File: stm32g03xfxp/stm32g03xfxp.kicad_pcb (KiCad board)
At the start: 2 copper layers, 17.8 x 33 mm, 17 parts, among them J1 USB2.0_C_v3, J3 ProMicro-RightPin, SW1 SW_Push, U1 AMS1117-3.3, U2 STM32G030F6P6

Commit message: up
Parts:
- added G***: LOGO, $74th:74th-5mm, B.Cu at (73.7, 49.0)
- added REF**: twitter, $74th:twitter, B.Cu at (73.9, 52.1)
- moved JP1 0.37 mm to (70.9, 48.3)
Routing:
- net RST: track 0.00 -> 49.8 mm, vias 0 -> 1
- net GND: track 0.00 -> 37.6 mm, vias 0 -> 28
- net 10/A10: track 0.00 -> 36.3 mm, vias 0 -> 2
- net 1/UART_TX: track 0.00 -> 24.4 mm, vias 0 -> 2
- net 0/UART_RX: track 0.00 -> 23.2 mm, vias 0 -> 2
- net 15/SPI_SCK: track 0.00 -> 21.2 mm
- net SWD_CLK: track 0.00 -> 19.2 mm, vias 0 -> 1
- net SWD_DIO: track 0.00 -> 18.5 mm, vias 0 -> 2
- net VCC: track 30.6 -> 48.3 mm
- net 18/A0: track 0.00 -> 15.7 mm, vias 0 -> 1
- net 2/I2C_SDA: track 0.00 -> 14.2 mm, vias 0 -> 1
- net 4/A6: track 0.00 -> 13.9 mm, vias 0 -> 1
- net 3/I2C_SCL: track 0.00 -> 13.5 mm, vias 0 -> 1
- net 6/A7: track 0.00 -> 10.7 mm, vias 0 -> 1
- net 19/A1: track 0.00 -> 10.4 mm
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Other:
- board text added: "3V"
- board text added: "5V"
- board text added: "A0"
- board text added: "A1"
- board text added: "A11"
- board text added: "A12"
- board text added: "A2"
- board text added: "A4"
- board text added: "A5"
- board text added: "A6"
- board text added: "A7"
- board text added: "B0"
- board text added: "B14"
- board text added: "B9"
- board text added: "C15"
- board text added: "CL"
- board text added: "DI"
- board text added: "G"
- board text added: "R"
- board text added: "RT"
- board text added: "SCL"
- board text added: "SDA"
- board text added: "STM32G03xFxP"
- board text added: "STM32G03xFxP ProMicro"
- board text added: "T"
- board text added: "v1.0.0"

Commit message: stm32g03xfxp/v1.0.0
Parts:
- added REF**: JLCJLCJLCJLC, $74th:JLCJLCJLCJLC, B.Cu at (65.4, 47.9)

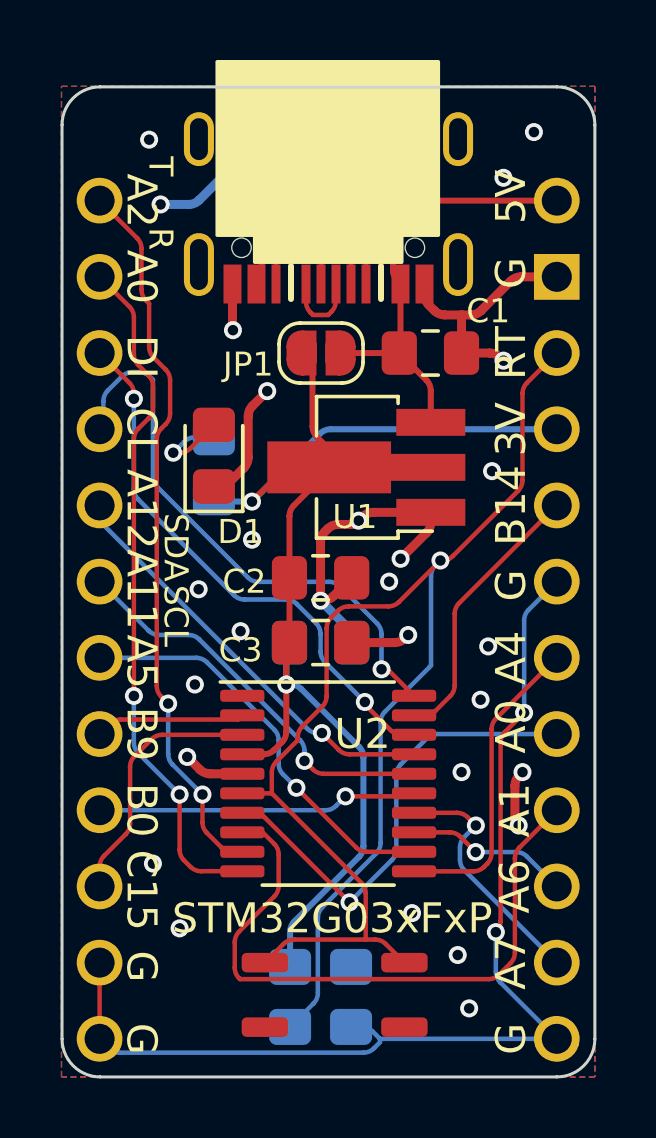
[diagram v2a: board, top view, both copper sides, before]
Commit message: fix dio/clk
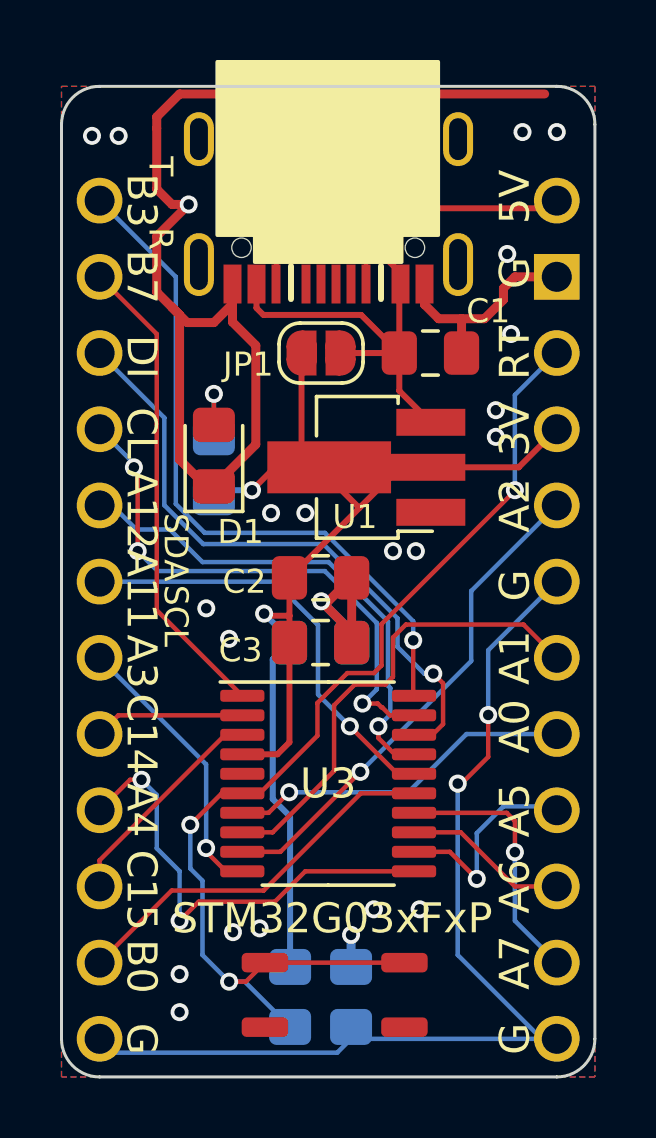
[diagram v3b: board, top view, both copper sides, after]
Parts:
- removed U2: STM32G030F6P6, Package_SO:TSSOP-20_4.4x6.5mm_P0.65mm
- added U3: STM32G030F6Px, Package_SO:TSSOP-20_4.4x6.5mm_P0.65mm, F.Cu at (71.1, 62.6)
- R1: value 200 -> 10k
- renumbered G*** to G1, REF** to T1, REF** to T2
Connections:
- CH1 pad 11: 10/A10 -> 8/A8
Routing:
- net GND: track 37.1 -> 57.6 mm, vias 28 -> 24
- net 15/SPI_SCK: track 21.3 -> 7.08 mm, vias 0 -> 1
- net RST: track 49.4 -> 36.6 mm, vias 1 -> 3
- net 8/A8: track 0.00 -> 12.8 mm
- net 21/A3: track 9.23 -> 16.6 mm, vias 0 -> 1
- net 0/UART_RX: track 23.0 -> 15.9 mm, vias 2 -> 0
- net 19/A1: track 10.3 -> 15.9 mm
- net 6/A7: track 10.7 -> 15.5 mm, vias 1 -> 2
- net 4/A6: track 13.8 -> 9.41 mm
- net 18/A0: track 15.6 -> 11.6 mm
- net VCC: track 48.0 -> 45.2 mm
- net unconnected-(J1-D+-Pad3): track 2.72 -> 0.00 mm
- net unconnected-(J1-D--Pad2): track 2.67 -> 0.00 mm
- net 2/I2C_SDA: track 14.2 -> 16.7 mm
- net SWD_DIO: track 18.3 -> 20.8 mm, vias 2 -> 1
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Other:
- outline, holes or cut-outs redrawn
- board text added: "A3"
- board text added: "B3"
- board text added: "B7"
- board text added: "C14"
- board text added: "v1.1.0"
- board text removed: "B14"
- board text removed: "B9"
- board text removed: "v1.0.0"

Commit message: v1.1.1
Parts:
- removed T1: JLCJLCJLCJLC, $74th:JLCJLCJLCJLC
- removed T2: twitter, $74th:twitter
- C3: moved to B.Cu
- D1: value LED -> Blue
- moved C4 7.71 mm to (73.2, 65.3)
- moved C3 4.89 mm to (73.2, 62.2)
- moved R2 3.56 mm to (72.8, 41.8)
- moved R1 3.56 mm to (69.2, 41.7)
- moved C2 1.66 mm to (72.5, 55.6)
- turned U2 to 180 degrees
- renumbered J3 to J2, R2 to R1, R3 to R2, R1 to R3, R5 to R4, R4 to R5, U3 to U2
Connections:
- U2 pad 5: unconnected-(U3-VSS-Pad5) -> GND
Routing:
- net GND: track 57.6 -> 40.8 mm, vias 24 -> 27
- net 5: track 5.01 -> 20.1 mm, vias 0 -> 1
- net 0/UART_RX: track 15.9 -> 26.5 mm, vias 0 -> 1
- net 15/SPI_SCK: track 7.08 -> 17.5 mm, vias 1 -> 0
- net 14/SPI_MISO: track 5.51 -> 15.6 mm
- net 19/A1: track 15.9 -> 6.05 mm
- net 7: track 7.36 -> 16.1 mm, vias 0 -> 2
- net 21/A3: track 16.6 -> 9.74 mm, vias 1 -> 0
- net 18/A0: track 11.6 -> 5.01 mm, vias 1 -> 0
- net 16/SPI_MOSI: track 8.77 -> 15.3 mm, vias 1 -> 0
- net VCC: track 45.2 -> 51.4 mm, vias 2 -> 6
- net 6/A7: track 15.5 -> 9.74 mm, vias 2 -> 1
- net 2/I2C_SDA: track 16.7 -> 12.9 mm
- net 3/I2C_SCL: track 14.5 -> 11.2 mm
- net 1/UART_TX: track 23.2 -> 26.4 mm, vias 1 -> 2
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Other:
- board text added: "RX"
- board text added: "SCK"
- board text added: "TX"
- board text added: "v1.1.1"
- board text removed: "v1.1.0"

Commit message: v1.2.0
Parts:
- removed JP1: SolderJumper_2_Open, Jumper:SolderJumper-2_P1.3mm_Open_RoundedPad1.0x1.5mm
- added J3: DAPLink-SWD-Recv-6Pin, $74th:BoxPinHeader_2x03_P1.27mm_Vertical, F.Cu at (71.2, 69.3)
- C1, C2, U1: moved to B.Cu
- moved G1 13.8 mm to (66.5, 60.8)
- moved C4 8.77 mm to (73.5, 56.5)
- moved D1 7.39 mm to (74.7, 51.1), turned to 180 degrees
- moved R3 7.04 mm to (74.3, 53.0)
- moved C1 6.37 mm to (68.2, 49.0), turned to 180 degrees
- moved SW1 6.03 mm to (71.2, 63.6)
- moved U2 5.59 mm to (71.1, 57.0)
- moved R4 3.20 mm to (75.1, 69.4)
- moved C2 3.05 mm to (69.6, 56.5), turned to 180 degrees
- moved U1 2.93 mm to (69.6, 53.0), turned to 0 degrees
- moved C3 2.82 mm to (73.6, 59.4)
- moved R5 2.31 mm to (67.6, 69.4)
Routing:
- net +5V: track 20.7 -> 48.1 mm, vias 0 -> 2
- net 4/A6: track 11.4 -> 34.3 mm
- net 6/A7: track 9.74 -> 25.6 mm, vias 1 -> 0
- net VCC: track 51.4 -> 38.7 mm, vias 6 -> 2
- net 5: track 20.1 -> 31.9 mm
- net 7: track 16.1 -> 26.2 mm, vias 2 -> 0
- net GND: track 40.8 -> 50.7 mm
- net SWD_DIO: track 18.5 -> 27.0 mm, vias 0 -> 2
- net 1/UART_TX: track 26.4 -> 34.4 mm
- net SWD_CLK: track 16.8 -> 24.3 mm, vias 0 -> 2
- net 0/UART_RX: track 26.5 -> 32.7 mm, vias 1 -> 0
- net 3/I2C_SCL: track 11.2 -> 5.83 mm
- net 10/A10: track 32.3 -> 36.8 mm
- net 21/A3: track 9.74 -> 5.40 mm
- net 2/I2C_SDA: track 12.9 -> 9.02 mm
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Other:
- board text added: "C"
- board text added: "SC"
- board text added: "v1.2.0"
- board text removed: "CL"
- board text removed: "RX"
- board text removed: "SCK"
- board text removed: "TX"
- board text removed: "v1.1.1"

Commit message: update README
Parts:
- added REF**: JLCJLCJLCJLC, $74th:JLCJLCJLCJLC, B.Cu at (65.0, 45.2)
- renumbered J2 to CH2, J3 to CH3
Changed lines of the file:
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@@
     (property "Sheetname" "")
     (attr through_hole)
-    (fp_text reference "J3" (at -1.83 -3.937) (layer "F.SilkS")
+    (fp_text reference "CH3" (at -1.83 -3.302) (layer "F.SilkS")
         (effects (font (size 1 1) (thickness 0.15)))
     )
@@
     (property "Sheetname" "")
     (attr through_hole)
-    (fp_text reference "J2" (at 0 -20.32 unlocked) (layer "F.SilkS") hide
+    (fp_text reference "CH2" (at 0 -20.32 unlocked) (layer "F.SilkS") hide
         (effects (font (size 1 1) (thickness 0.15)))
     )
-    (fp_text value "ProMicro-RightPin" (at -25.425 -21.229 unlocked) (layer "F.Fab")
+    (fp_text value "ProMicro-RightPin" (at -0.127 -20.955 unlocked) (layer "F.Fab")
         (effects (font (size 1 1) (thickness 0.15)))
     )
@@
     (fp_line (start 1 0.6) (end 1 -0.6)
       (stroke (width 0.1) (type solid)) (layer "F.Fab"))
-    (pad "1" smd roundrect (at -1.025 0 180) (size 1.15 1.4) (layers "F.Cu" "F.Paste" "F.Mask") (roundrect_rratio 0.217391)
+    (pad "1" smd roundrect (at -1.025 0 180) (size 1.15 1.4) (layers "F.Cu" "F.Paste" "F.Mask") (roundrect_rratio 0.2173913043)
       (net 2 "GND") (pinfunction "K") (pintype "passive"))
-    (pad "2" smd roundrect (at 1.025 0 180) (size 1.15 1.4) (layers "F.Cu" "F.Paste" "F.Mask") (roundrect_rratio 0.217391)
+    (pad "2" smd roundrect (at 1.025 0 180) (size 1.15 1.4) (layers "F.Cu" "F.Paste" "F.Mask") (roundrect_rratio 0.2173913043)
       (net 5 "Net-(D1-A)") (pinfunction "A") (pintype "passive"))
     (model "${KICAD6_3DMODEL_DIR}/LED_SMD.3dshapes/LED_0805_2012Metric.wrl"
@@
       (scale (xyz 1 1 1))
       (rotate (xyz -90 0 0))
+    )
+  )
+  (footprint "$74th:JLCJLCJLCJLC" (layer "B.Cu")
+    (at 65.024 45.212 90)
+    (attr smd)
+    (fp_text reference "REF**" (at 0 1.6 270 unlocked) (layer "B.SilkS") hide
+        (effects (font (size 1 1) (thickness 0.15)) (justify mirror))
+    )
+    (fp_text value "JLCJLCJLCJLC" (at 0 0 270 unlocked) (layer "B.SilkS")
+        (effects (font (size 0.8 0.8) (thickness 0.15)) (justify mirror))
     )
   )
@@
     (fp_rect (start -1.88 0.98) (end 1.88 -0.98)
       (stroke (width 0.05) (type default)) (fill none) (layer "B.CrtYd"))
-    (pad "1" smd roundrect (at -1.0375 0 180) (size 1.175 1.45) (layers "B.Cu" "B.Paste" "B.Mask") (roundrect_rratio 0.212766)
+    (pad "1" smd roundrect (at -1.0375 0 180) (size 1.175 1.45) (layers "B.Cu" "B.Paste" "B.Mask") (roundrect_rratio 0.2127659574)
       (net 3 "VCC") (pintype "passive"))
-    (pad "2" smd roundrect (at 1.0375 0 180) (size 1.175 1.45) (layers "B.Cu" "B.Paste" "B.Mask") (roundrect_rratio 0.212766)
+    (pad "2" smd roundrect (at 1.0375 0 180) (size 1.175 1.45) (layers "B.Cu" "B.Paste" "B.Mask") (roundrect_rratio 0.2127659574)
       (net 2 "GND") (pintype "passive"))
     (model "${KICAD6_3DMODEL_DIR}/Capacitor_SMD.3dshapes/C_0805_2012Metric.wrl"
@@
     (fp_rect (start -1.88 0.98) (end 1.88 -0.98)
       (stroke (width 0.05) (type default)) (fill none) (layer "B.CrtYd"))
-    (pad "1" smd roundrect (at -1 0 90) (size 1.2 1.4) (layers "B.Cu" "B.Paste" "B.Mask") (roundrect_rratio 0.208333)
+    (pad "1" smd roundrect (at -1 0 90) (size 1.2 1.4) (layers "B.Cu" "B.Paste" "B.Mask") (roundrect_rratio 0.2083333333)
       (net 10 "10{slash}A10") (pintype "passive"))
-    (pad "2" smd roundrect (at 1 0 90) (size 1.2 1.4) (layers "B.Cu" "B.Paste" "B.Mask") (roundrect_rratio 0.208333)
+    (pad "2" smd roundrect (at 1 0 90) (size 1.2 1.4) (layers "B.Cu" "B.Paste" "B.Mask") (roundrect_rratio 0.2083333333)
       (net 2 "GND") (pintype "passive"))
     (model "${KICAD6_3DMODEL_DIR}/Resistor_SMD.3dshapes/R_0805_2012Metric.wrl"
@@
     (fp_rect (start -1.88 0.98) (end 1.88 -0.98)
       (stroke (width 0.05) (type default)) (fill none) (layer "B.CrtYd"))
-    (pad "1" smd roundrect (at -1.0375 0) (size 1.175 1.45) (layers "B.Cu" "B.Paste" "B.Mask") (roundrect_rratio 0.212766)
+    (pad "1" smd roundrect (at -1.0375 0) (size 1.175 1.45) (layers "B.Cu" "B.Paste" "B.Mask") (roundrect_rratio 0.2127659574)
       (net 3 "VCC") (pintype "passive"))
-    (pad "2" smd roundrect (at 1.0375 0) (size 1.175 1.45) (layers "B.Cu" "B.Paste" "B.Mask") (roundrect_rratio 0.212766)
+    (pad "2" smd roundrect (at 1.0375 0) (size 1.175 1.45) (layers "B.Cu" "B.Paste" "B.Mask") (roundrect_rratio 0.2127659574)
       (net 2 "GND") (pintype "passive"))
     (model "${KICAD6_3DMODEL_DIR}/Capacitor_SMD.3dshapes/C_0805_2012Metric.wrl"
@@
     (fp_rect (start -1.88 0.98) (end 1.88 -0.98)
       (stroke (width 0.05) (type default)) (fill none) (layer "B.CrtYd"))
-    (pad "1" smd roundrect (at -1 0 270) (size 1.2 1.4) (layers "B.Cu" "B.Paste" "B.Mask") (roundrect_rratio 0.208333)
+    (pad "1" smd roundrect (at -1 0 270) (size 1.2 1.4) (layers "B.Cu" "B.Paste" "B.Mask") (roundrect_rratio 0.2083333333)
       (net 3 "VCC") (pintype "passive"))
-    (pad "2" smd roundrect (at 1 0 270) (size 1.2 1.4) (layers "B.Cu" "B.Paste" "B.Mask") (roundrect_rratio 0.208333)
+    (pad "2" smd roundrect (at 1 0 270) (size 1.2 1.4) (layers "B.Cu" "B.Paste" "B.Mask") (roundrect_rratio 0.2083333333)
       (net 4 "RST") (pintype "passive"))
     (model "${KICAD6_3DMODEL_DIR}/Resistor_SMD.3dshapes/R_0805_2012Metric.wrl"
@@
     (fp_rect (start -1.88 0.98) (end 1.88 -0.98)
       (stroke (width 0.05) (type default)) (fill none) (layer "B.CrtYd"))
-    (pad "1" smd roundrect (at -1 0 90) (size 1.2 1.4) (layers "B.Cu" "B.Paste" "B.Mask") (roundrect_rratio 0.208333)
+    (pad "1" smd roundrect (at -1 0 90) (size 1.2 1.4) (layers "B.Cu" "B.Paste" "B.Mask") (roundrect_rratio 0.2083333333)
       (net 3 "VCC") (pintype "passive"))
-    (pad "2" smd roundrect (at 1 0 90) (size 1.2 1.4) (layers "B.Cu" "B.Paste" "B.Mask") (roundrect_rratio 0.208333)
+    (pad "2" smd roundrect (at 1 0 90) (size 1.2 1.4) (layers "B.Cu" "B.Paste" "B.Mask") (roundrect_rratio 0.2083333333)
       (net 5 "Net-(D1-A)") (pintype "passive"))
     (model "${KICAD6_3DMODEL_DIR}/Resistor_SMD.3dshapes/R_0805_2012Metric.wrl"
@@
     (fp_rect (start -1.88 0.98) (end 1.88 -0.98)
       (stroke (width 0.05) (type default)) (fill none) (layer "B.CrtYd"))
-    (pad "1" smd roundrect (at -1 0 90) (size 1.2 1.4) (layers "B.Cu" "B.Paste" "B.Mask") (roundrect_rratio 0.208333)
+    (pad "1" smd roundrect (at -1 0 90) (size 1.2 1.4) (layers "B.Cu" "B.Paste" "B.Mask") (roundrect_rratio 0.2083333333)
       (net 8 "Net-(J1-CC1)") (pintype "passive"))
-    (pad "2" smd roundrect (at 1 0 90) (size 1.2 1.4) (layers "B.Cu" "B.Paste" "B.Mask") (roundrect_rratio 0.208333)
+    (pad "2" smd roundrect (at 1 0 90) (size 1.2 1.4) (layers "B.Cu" "B.Paste" "B.Mask") (roundrect_rratio 0.2083333333)
       (net 2 "GND") (pintype "passive"))
     (model "${KICAD6_3DMODEL_DIR}/Resistor_SMD.3dshapes/R_0805_2012Metric.wrl"
@@
     (fp_rect (start -1.88 0.98) (end 1.88 -0.98)
       (stroke (width 0.05) (type default)) (fill none) (layer "B.CrtYd"))
-    (pad "1" smd roundrect (at -1.0375 0) (size 1.175 1.45) (layers "B.Cu" "B.Paste" "B.Mask") (roundrect_rratio 0.212766)
+    (pad "1" smd roundrect (at -1.0375 0) (size 1.175 1.45) (layers "B.Cu" "B.Paste" "B.Mask") (roundrect_rratio 0.2127659574)
       (net 3 "VCC") (pintype "passive"))
-    (pad "2" smd roundrect (at 1.0375 0) (size 1.175 1.45) (layers "B.Cu" "B.Paste" "B.Mask") (roundrect_rratio 0.212766)
+    (pad "2" smd roundrect (at 1.0375 0) (size 1.175 1.45) (layers "B.Cu" "B.Paste" "B.Mask") (roundrect_rratio 0.2127659574)
       (net 2 "GND") (pintype "passive"))
     (model "${KICAD6_3DMODEL_DIR}/Capacitor_SMD.3dshapes/C_0805_2012Metric.wrl"
@@
     (fp_rect (start -1.88 0.98) (end 1.88 -0.98)
       (stroke (width 0.05) (type default)) (fill none) (layer "B.CrtYd"))
-    (pad "1" smd roundrect (at -1.0375 0 180) (size 1.175 1.45) (layers "B.Cu" "B.Paste" "B.Mask") (roundrect_rratio 0.212766)
+    (pad "1" smd roundrect (at -1.0375 0 180) (size 1.175 1.45) (layers "B.Cu" "B.Paste" "B.Mask") (roundrect_rratio 0.2127659574)
       (net 1 "+5V") (pintype "passive"))
-    (pad "2" smd roundrect (at 1.0375 0 180) (size 1.175 1.45) (layers "B.Cu" "B.Paste" "B.Mask") (roundrect_rratio 0.212766)
+    (pad "2" smd roundrect (at 1.0375 0 180) (size 1.175 1.45) (layers "B.Cu" "B.Paste" "B.Mask") (roundrect_rratio 0.2127659574)
       (net 2 "GND") (pintype "passive"))
     (model "${KICAD6_3DMODEL_DIR}/Capacitor_SMD.3dshapes/C_0805_2012Metric.wrl"
@@
     (fp_rect (start -1.88 0.98) (end 1.88 -0.98)
       (stroke (width 0.05) (type default)) (fill none) (layer "B.CrtYd"))
-    (pad "1" smd roundrect (at -1 0 90) (size 1.2 1.4) (layers "B.Cu" "B.Paste" "B.Mask") (roundrect_rratio 0.208333)
+    (pad "1" smd roundrect (at -1 0 90) (size 1.2 1.4) (layers "B.Cu" "B.Paste" "B.Mask") (roundrect_rratio 0.2083333333)
       (net 9 "Net-(J1-CC2)") (pintype "passive"))
-    (pad "2" smd roundrect (at 1 0 90) (size 1.2 1.4) (layers "B.Cu" "B.Paste" "B.Mask") (roundrect_rratio 0.208333)
+    (pad "2" smd roundrect (at 1 0 90) (size 1.2 1.4) (layers "B.Cu" "B.Paste" "B.Mask") (roundrect_rratio 0.2083333333)
       (net 2 "GND") (pintype "passive"))
     (model "${KICAD6_3DMODEL_DIR}/Resistor_SMD.3dshapes/R_0805_2012Metric.wrl"

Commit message: stm32g03xfxp/v1.2.0
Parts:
- removed CH3: DAPLink-SWD-Recv-6Pin, $74th:BoxPinHeader_2x03_P1.27mm_Vertical
- removed R4: 0, $74th:Register_0805_2012
- added J2: SWD-MCU_Side-10Pin, $74th:SWD_2x05_P1.27mm, F.Cu at (68.4, 50.7)
- U1: moved to F.Cu
- moved D1 20.0 mm to (66.9, 69.5), turned to 90 degrees
- moved R3 17.9 mm to (67.2, 69.4)
- moved C1 6.78 mm to (73.7, 52.9)
- moved SW1 5.91 mm to (71.8, 69.5)
- moved U2 5.11 mm to (71.2, 62.1), turned to 0 degrees
- moved C3 4.64 mm to (69.2, 57.7), turned to 180 degrees
- moved U1 2.36 mm to (70.7, 55.0), turned to 180 degrees
- moved C2 1.93 mm to (69.3, 54.6)
- moved R5 1.84 mm to (69.4, 69.5), turned to 90 degrees
- moved C4 1.33 mm to (73.1, 57.8)
- moved R1 0.38 mm to (69.6, 41.7)
- moved R2 0.22 mm to (72.6, 41.7)
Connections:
- net 0/UART_RX renamed /0/UART_RX
- net 14/SPI_MISO renamed /14/API_MISO
- net 15/SPI_SCK renamed /15/SPI_SCK
- net 16/SPI_MOSI renamed /16/SPI_MOSI
- net 1/UART_TX renamed /1/UART_TX
- net 2/I2C_SDA renamed /2/I2C_SDA
- net 3/I2C_SCL renamed /3/I2C_SCL
- net RST renamed /RST
- net SWD_CLK renamed /SWCLK
- net SWD_DIO renamed /SWDIO
- net VCC renamed +3V3
- CH1 pad 10: 7 -> /7
- CH1 pad 11: 8/A8 -> /8/A8
- CH1 pad 12: 10/A10 -> GND
- CH1 pad 7: 4/A6 -> /4/A6
- CH1 pad 8: 5 -> /5
- CH1 pad 9: 6/A7 -> /6/A7
- CH2 pad 1: 10/A10 -> GND
- CH2 pad 5: 18/A0 -> /18/A0
- CH2 pad 6: 19/A1 -> /19/A1
- CH2 pad 7: 10/A10 -> GND
- CH2 pad 8: 21/A3 -> /21/A3
- U2 pad 10: 4/A6 -> /18/A0
- U2 pad 11: 6/A7 -> /19/A1
- U2 pad 15: 8/A8 -> /21/A3
- U2 pad 2: 5 -> /4/A6
- U2 pad 3: 7 -> /5
- U2 pad 7: 18/A0 -> /6/A7
- U2 pad 8: 19/A1 -> /7
- U2 pad 9: 21/A3 -> /8/A8
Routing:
- net 10/A10: track 36.8 -> 0.00 mm
- net 4/A6: track 34.3 -> 0.00 mm, vias 1 -> 0
- net 5: track 31.9 -> 0.00 mm, vias 1 -> 0
- net 7: track 26.2 -> 0.00 mm
- net 6/A7: track 25.6 -> 0.00 mm
- net +5V: track 48.1 -> 30.3 mm
- net 8/A8: track 14.7 -> 0.00 mm, vias 1 -> 0
- net /18/A0: track 0.00 -> 12.3 mm, vias 0 -> 2
- net /21/A3: track 0.00 -> 11.5 mm, vias 0 -> 2
- net /19/A1: track 0.00 -> 10.6 mm, vias 0 -> 1
- net /15/SPI_SCK: track 15.1 -> 5.06 mm, vias 1 -> 0
- net /16/SPI_MOSI: track 18.0 -> 8.76 mm
- net /14/API_MISO: track 17.2 -> 8.29 mm
- net /3/I2C_SCL: track 5.83 -> 14.4 mm
- net 18/A0: track 7.23 -> 0.00 mm
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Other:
- board text added: "DIO"
- board text added: "SPI"
- board text added: "SWD"
- board text added: "v1.3.0"
- board text removed: "DI"
- board text removed: "SC"
- board text removed: "v1.2.0"

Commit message: stm32g03xfxp/v1.3.0
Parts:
- renumbered R2 to R1, R1 to R2, R5 to R4
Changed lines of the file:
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@@
     (property "ki_keywords" "R res resistor")
     (attr smd)
-    (fp_text reference "R5" (at 1.1176 1.8034) (layer "B.SilkS")
+    (fp_text reference "R4" (at 1.1176 1.8034) (layer "B.SilkS")
         (effects (font (size 0.8 0.8) (thickness 0.12)) (justify mirror))
     )
@@
     (property "ki_keywords" "R res resistor")
     (attr smd)
-    (fp_text reference "R2" (at -1.2954 1.8796 180) (layer "B.SilkS")
+    (fp_text reference "R1" (at -1.2954 1.8796 180) (layer "B.SilkS")
         (effects (font (size 0.8 0.8) (thickness 0.12)) (justify mirror))
     )
@@
     (property "ki_keywords" "R res resistor")
     (attr smd)
-    (fp_text reference "R1" (at -1.4478 -1.8288 180) (layer "B.SilkS")
+    (fp_text reference "R2" (at -1.4478 -1.8288 180) (layer "B.SilkS")
         (effects (font (size 0.8 0.8) (thickness 0.12)) (justify mirror))
     )
